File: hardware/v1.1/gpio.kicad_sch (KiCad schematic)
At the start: 23 parts, among them J2 HDMI_C_1.3, U1 ECP5U_12_CABGA256, U5 PCA9306DC1

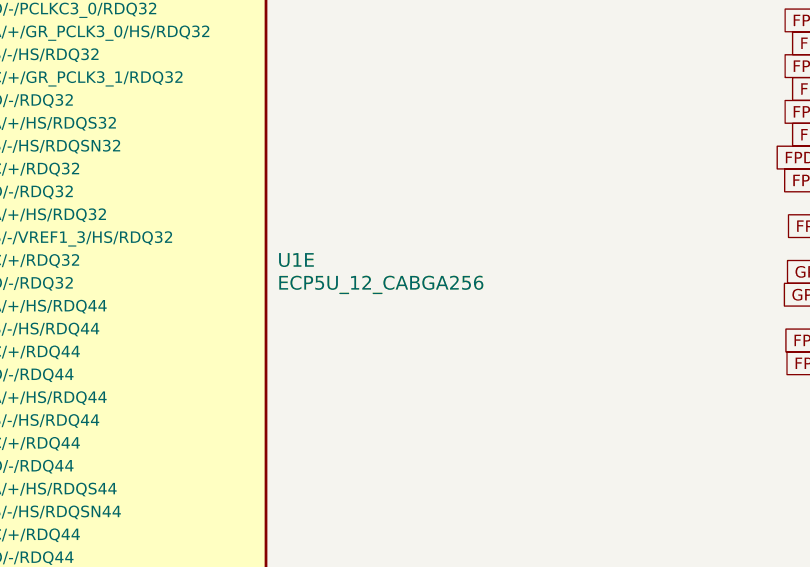
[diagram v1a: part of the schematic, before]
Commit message: Clean up the design by a bit
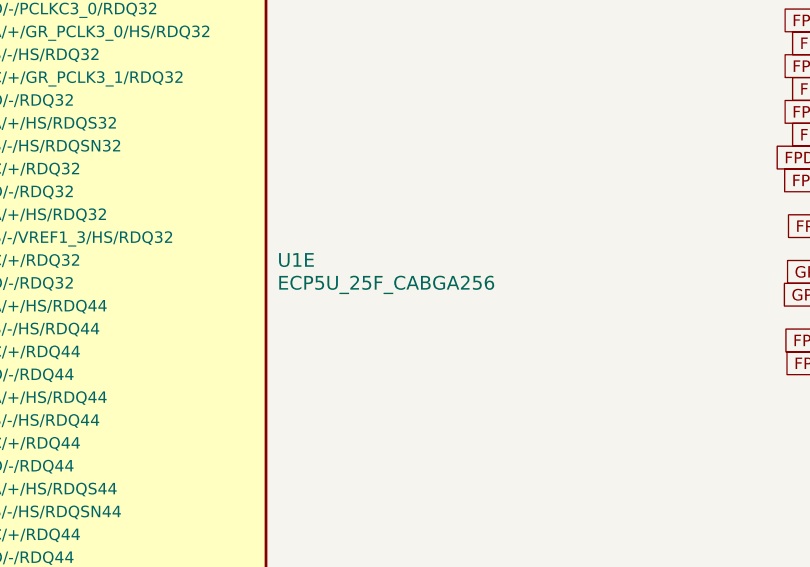
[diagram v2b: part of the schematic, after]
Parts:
- U1: value ECP5U_12_CABGA256 -> ECP5U_25F_CABGA256
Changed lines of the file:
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@@
 			)
 		)
-		(property "Value" "ECP5U_12_CABGA256"
+		(property "Value" "ECP5U_25F_CABGA256"
 			(at 104.14 100.3299 0)
 			(effects

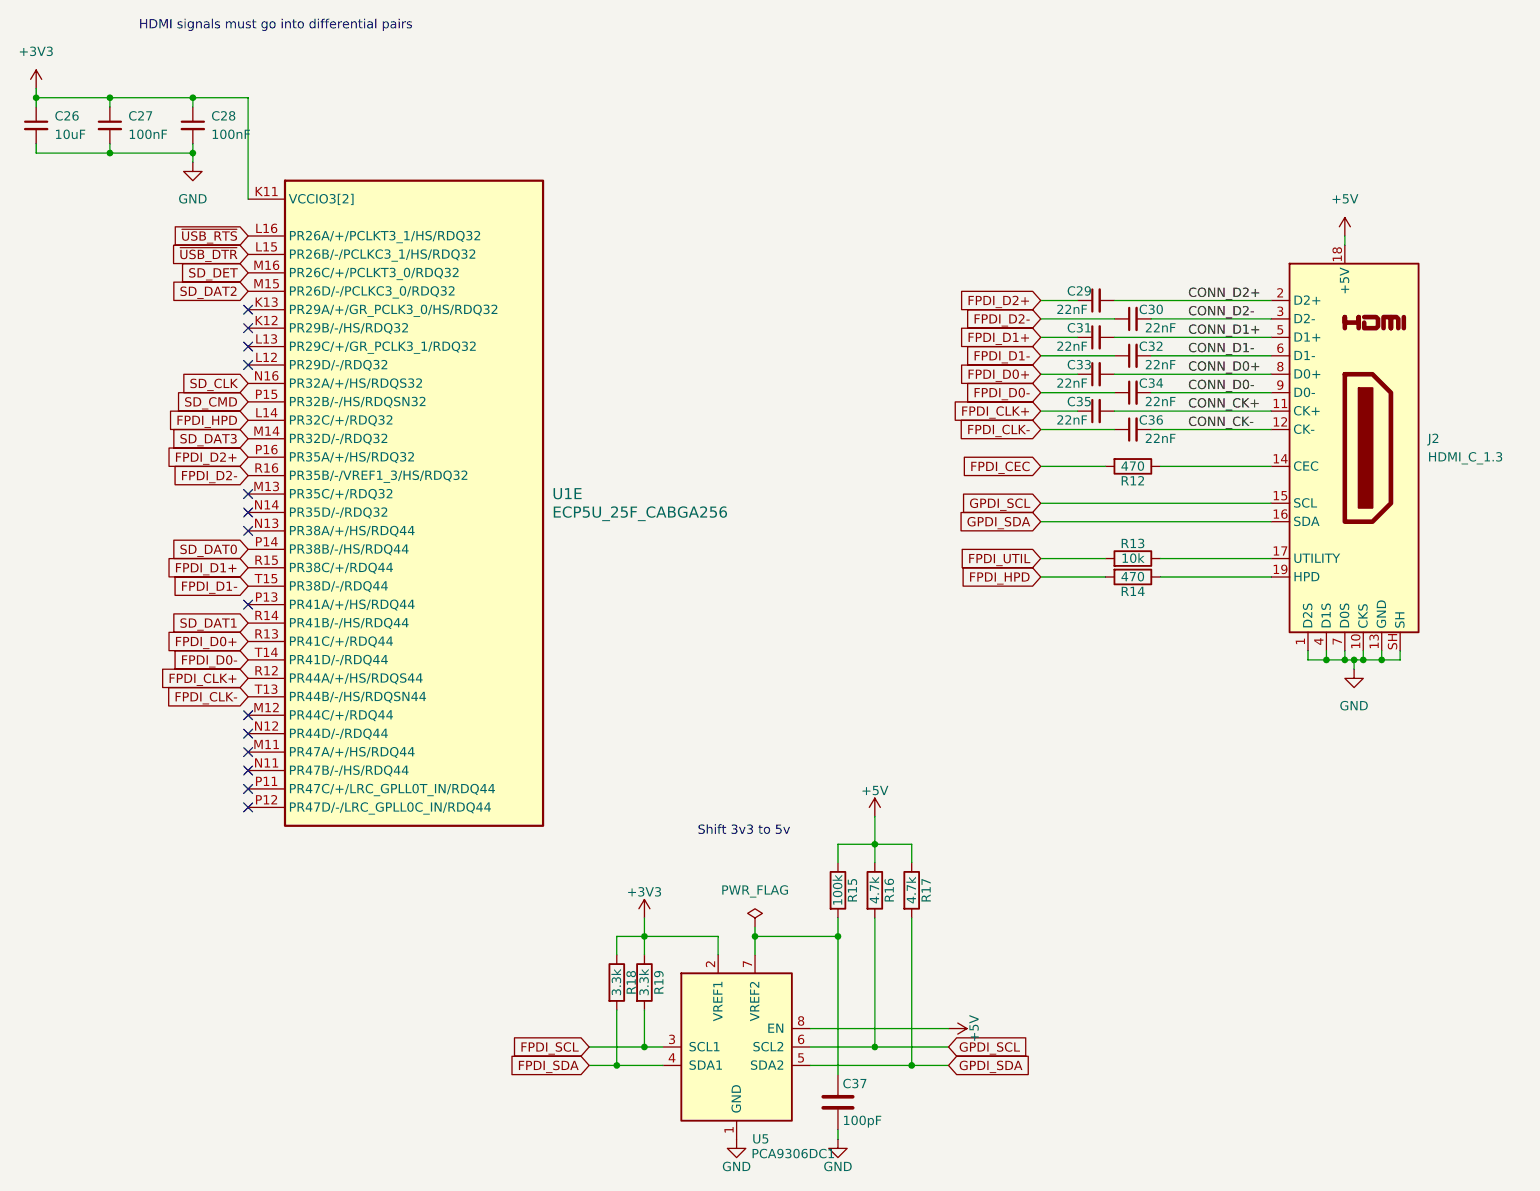
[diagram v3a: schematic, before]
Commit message: Fix pin assignment errors and schematic lable naming mismatch between versions
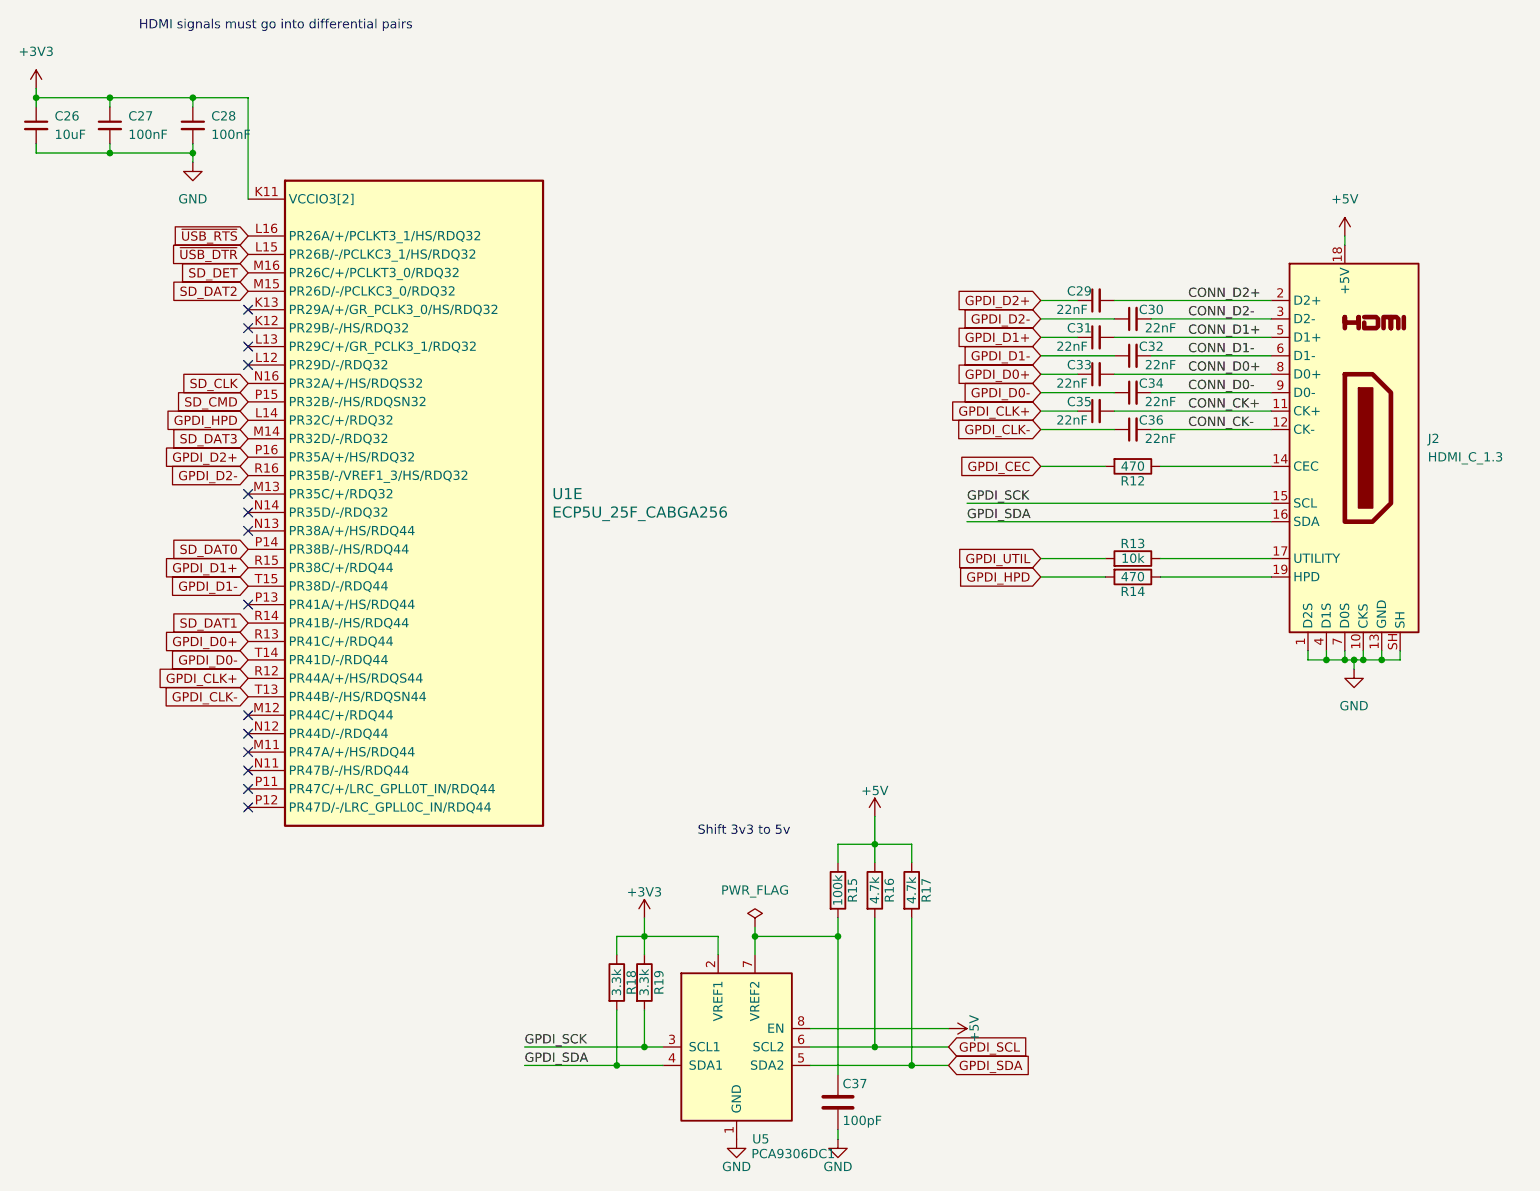
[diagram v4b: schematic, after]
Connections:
- net FPDI_SDA is gone; now on net GPDI_SDA: R18.2, U5.4 (SDA1)
- net GPDI_SCL: no longer J2.15 (SCL)
- net FPDI_CEC renamed GPDI_CEC
- net FPDI_CLK+ renamed GPDI_CLK+
- net FPDI_CLK- renamed GPDI_CLK-
- net FPDI_D0+ renamed GPDI_D0+
- net FPDI_D0- renamed GPDI_D0-
- net FPDI_D1+ renamed GPDI_D1+
- net FPDI_D1- renamed GPDI_D1-
- net FPDI_D2+ renamed GPDI_D2+
- net FPDI_D2- renamed GPDI_D2-
- net FPDI_HPD renamed GPDI_HPD
- net FPDI_SCL renamed GPDI_SCK
- net GPDI_SCK: now also J2.15 (SCL)
- net FPDI_UTIL renamed GPDI_UTIL

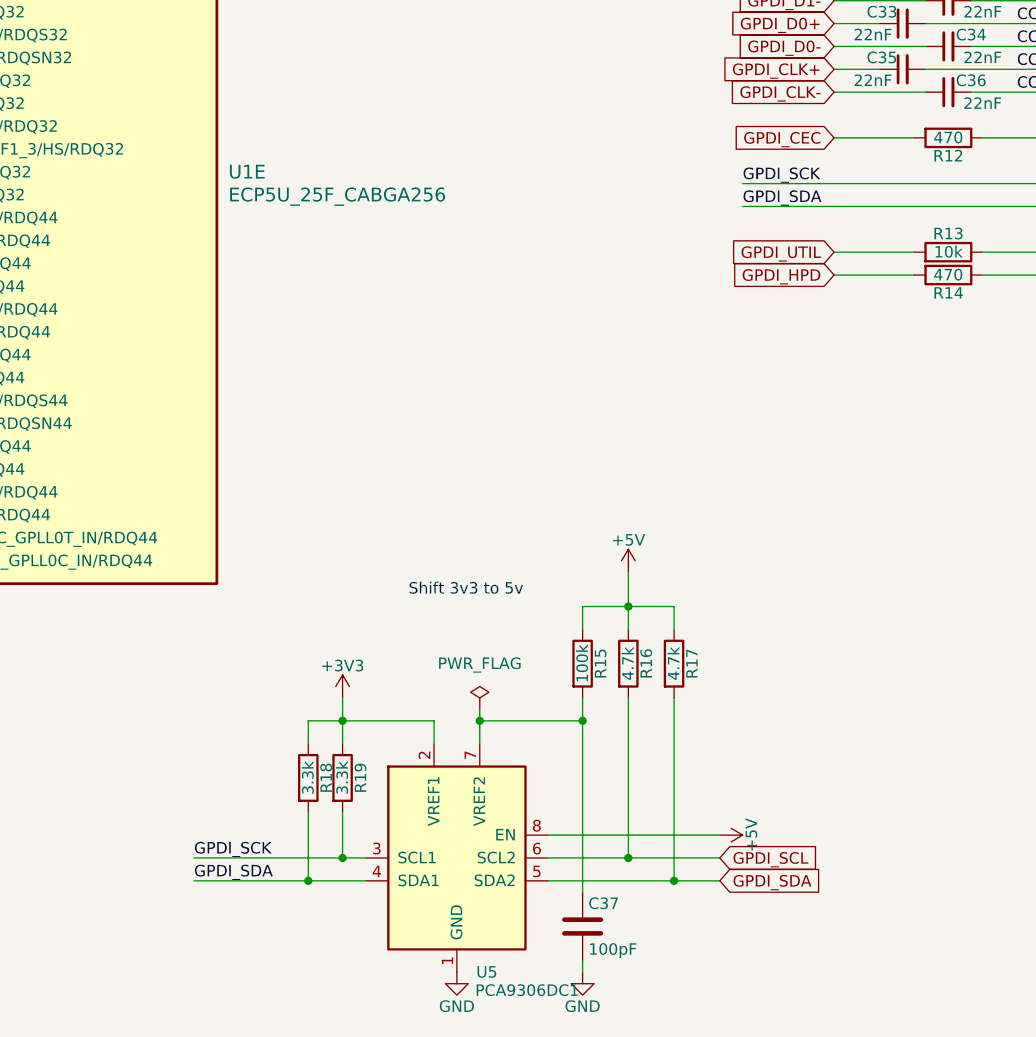
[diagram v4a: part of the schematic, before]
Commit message: Increase pad spacing to 1.9mm and change SCL name to SCK
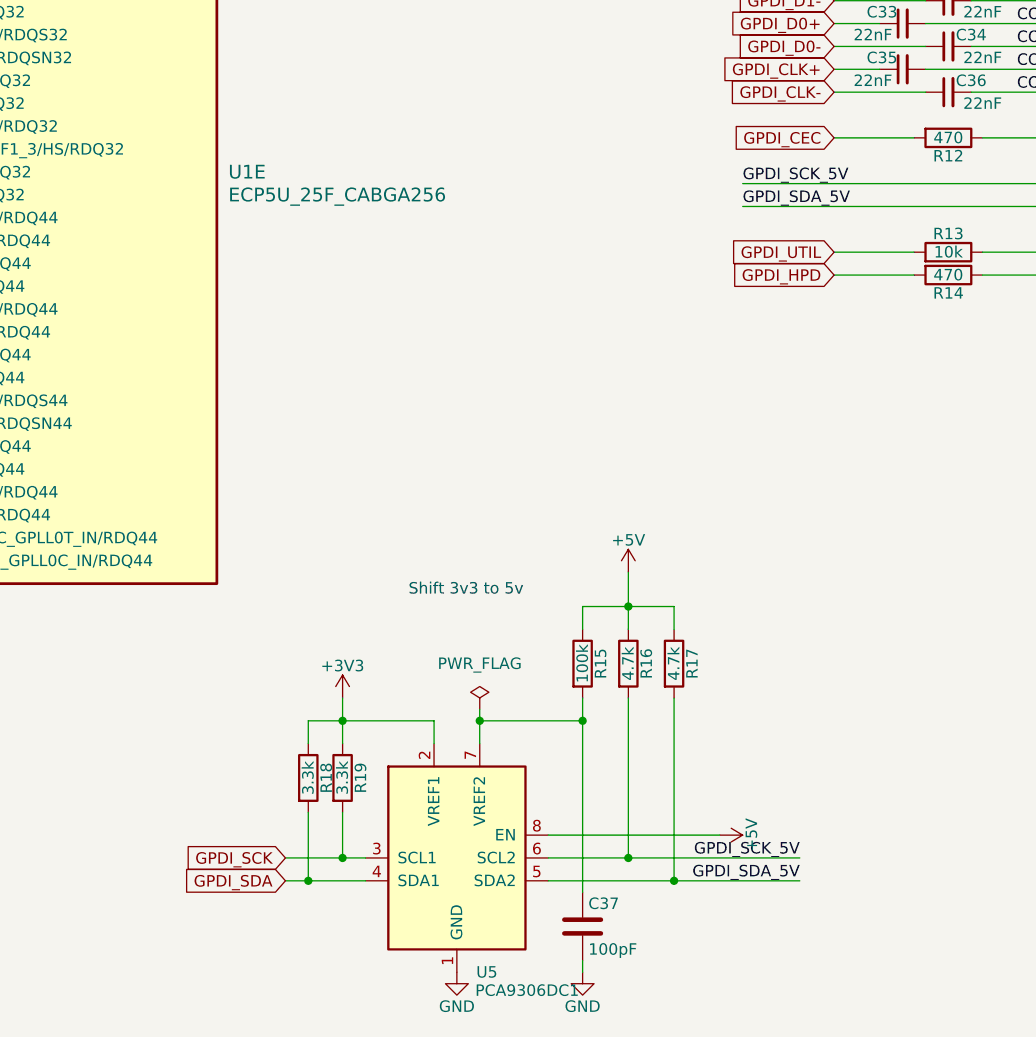
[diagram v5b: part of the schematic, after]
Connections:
- net GPDI_SCK: no longer J2.15 (SCL)
- net GPDI_SDA: no longer J2.16 (SDA), R17.2, U5.5 (SDA2)
- net GPDI_SCL renamed GPDI_SCK_5V
- net GPDI_SCK_5V: now also J2.15 (SCL)
- new net GPDI_SDA_5V: J2.16 (SDA), R17.2, U5.5 (SDA2)
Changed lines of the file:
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@@
 	(title_block
 		(title "Icepi zero")
-		(date "2025-06-06")
+		(date "2025-06-11")
 		(rev "v1.1")
 		(company "Chengyin Yao (cheyao)")
@@
 	)
 	(junction
+		(at 143.51 158.75)
+		(diameter 0)
+		(color 0 0 0 0)
+	)
+	(junction
+		(at 210.82 120.65)
+		(diameter 0)
+		(color 0 0 0 0)
+	)
+	(junction
+		(at 113.03 176.53)
+		(diameter 0)
+		(color 0 0 0 0)
+	)
+	(junction
+		(at 148.59 146.05)
+		(diameter 0)
+		(color 0 0 0 0)
+	)
+	(junction
+		(at 132.08 158.75)
+		(diameter 0)
+		(color 0 0 0 0)
+	)
+	(junction
+		(at 214.63 120.65)
+		(diameter 0)
+		(color 0 0 0 0)
+	)
+	(junction
+		(at 43.18 43.18)
+		(diameter 0)
+		(color 0 0 0 0)
+	)
+	(junction
+		(at 218.44 120.65)
+		(diameter 0)
+		(color 0 0 0 0)
+	)
+	(junction
+		(at 54.61 43.18)
+		(diameter 0)
+		(color 0 0 0 0)
+	)
+	(junction
 		(at 116.84 173.99)
-		(diameter 0)
-		(color 0 0 0 0)
-	)
-	(junction
-		(at 143.51 158.75)
-		(diameter 0)
-		(color 0 0 0 0)
-	)
-	(junction
-		(at 210.82 120.65)
-		(diameter 0)
-		(color 0 0 0 0)
-	)
-	(junction
-		(at 113.03 176.53)
-		(diameter 0)
-		(color 0 0 0 0)
-	)
-	(junction
-		(at 148.59 146.05)
-		(diameter 0)
-		(color 0 0 0 0)
-	)
-	(junction
-		(at 132.08 158.75)
-		(diameter 0)
-		(color 0 0 0 0)
-	)
-	(junction
-		(at 214.63 120.65)
-		(diameter 0)
-		(color 0 0 0 0)
-	)
-	(junction
-		(at 43.18 43.18)
-		(diameter 0)
-		(color 0 0 0 0)
-	)
-	(junction
-		(at 218.44 120.65)
-		(diameter 0)
-		(color 0 0 0 0)
-	)
-	(junction
-		(at 54.61 43.18)
 		(diameter 0)
 		(color 0 0 0 0)
@@
 	(wire
 		(pts
-			(xy 148.59 173.99) (xy 158.75 173.99)
+			(xy 148.59 173.99) (xy 167.64 173.99)
 		)
 		(stroke
@@
 	(wire
 		(pts
-			(xy 153.67 176.53) (xy 158.75 176.53)
-		)
-		(stroke
-			(width 0)
-			(type default)
-		)
-	)
-	(wire
-		(pts
 			(xy 171.45 86.36) (xy 176.53 86.36)
 		)
@@
 	(wire
 		(pts
+			(xy 110.49 176.53) (xy 113.03 176.53)
+		)
+		(stroke
+			(width 0)
+			(type default)
+		)
+	)
+	(wire
+		(pts
 			(xy 218.44 120.65) (xy 220.98 120.65)
 		)
@@
 	(wire
 		(pts
-			(xy 100.33 176.53) (xy 113.03 176.53)
+			(xy 153.67 176.53) (xy 167.64 176.53)
 		)
 		(stroke
@@
 	(wire
 		(pts
+			(xy 110.49 173.99) (xy 116.84 173.99)
+		)
+		(stroke
+			(width 0)
+			(type default)
+		)
+	)
+	(wire
+		(pts
 			(xy 54.61 50.8) (xy 54.61 49.53)
 		)
@@
 	(wire
 		(pts
-			(xy 100.33 173.99) (xy 116.84 173.99)
-		)
-		(stroke
-			(width 0)
-			(type default)
-		)
-	)
-	(wire
-		(pts
 			(xy 153.67 146.05) (xy 153.67 148.59)
 		)
@@
 		)
 	)
-	(label "GPDI_SCK"
-		(at 100.33 173.99 0)
-		(effects
-			(font
-				(size 1.27 1.27)
-			)
-			(justify left bottom)
+	(label "GPDI_SCK_5V"
+		(at 167.64 173.99 180)
+		(effects
+			(font
+				(size 1.27 1.27)
+			)
+			(justify right bottom)
 		)
 	)
@@
 		)
 	)
-	(label "GPDI_SDA"
-		(at 100.33 176.53 0)
-		(effects
-			(font
-				(size 1.27 1.27)
-			)
-			(justify left bottom)
-		)
-	)
-	(label "GPDI_SCK"
+	(label "GPDI_SDA_5V"
+		(at 167.64 176.53 180)
+		(effects
+			(font
+				(size 1.27 1.27)
+			)
+			(justify right bottom)
+		)
+	)
+	(label "GPDI_SCK_5V"
 		(at 161.29 99.06 0)
 		(effects
@@
 		)
 	)
-	(label "GPDI_SDA"
+	(label "GPDI_SDA_5V"
 		(at 161.29 101.6 0)
 		(effects
@@
 	(global_label "GPDI_SDA"
 		(shape input)
-		(at 158.75 176.53 0)
-		(effects
-			(font
-				(size 1.27 1.27)
-			)
-			(justify left)
-		)
-		(property "Intersheetrefs" "${INTERSHEET_REFS}"
-			(at 158.75 176.53 0)
+		(at 110.49 176.53 180)
+		(effects
+			(font
+				(size 1.27 1.27)
+			)
+			(justify right)
+		)
+		(property "Intersheetrefs" "${INTERSHEET_REFS}"
+			(at 110.49 176.53 0)
 			(effects
 				(font
@@
 		)
 	)
-	(global_label "GPDI_SCL"
-		(shape input)
-		(at 158.75 173.99 0)
-		(effects
-			(font
-				(size 1.27 1.27)
-			)
-			(justify left)
-		)
-		(property "Intersheetrefs" "${INTERSHEET_REFS}"
-			(at 158.75 173.99 0)
-			(effects
-				(font
+	(global_label "GPDI_SCK"
+		(shape input)
+		(at 110.49 173.99 180)
+		(effects
+			(font
+				(size 1.27 1.27)
+			)
+			(justify right)
+		)
+		(property "Intersheetrefs" "${INTERSHEET_REFS}"
+			(at 110.49 173.99 0)
+			(effects
+				(font

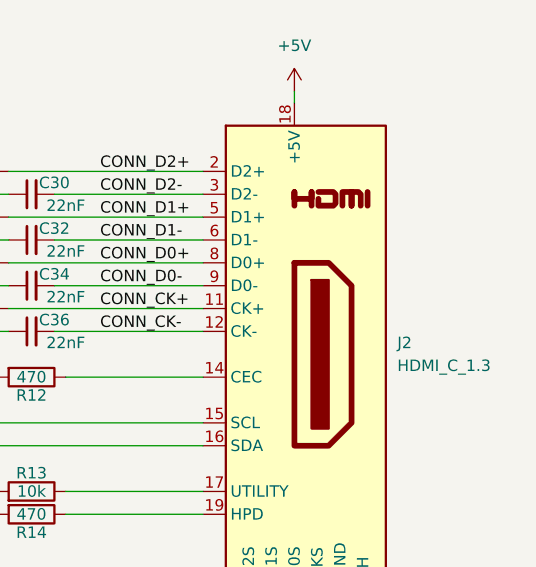
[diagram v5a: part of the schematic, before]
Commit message: Added start of documentation and changed GPDI
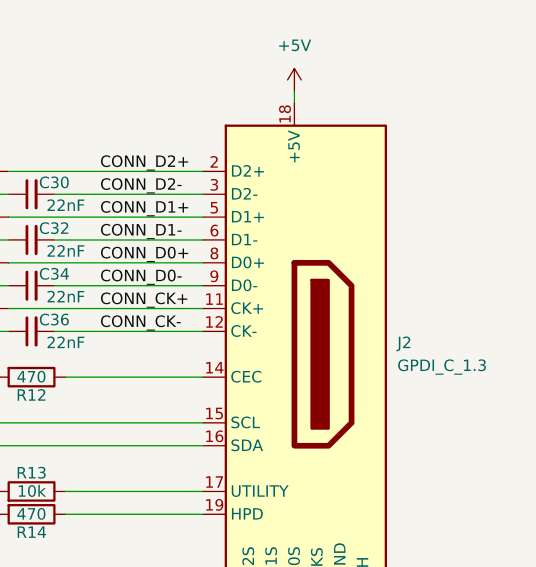
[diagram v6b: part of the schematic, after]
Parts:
- J2: value HDMI_C_1.3 -> GPDI_C_1.3; symbol Connector:HDMI_C_1.3 -> icepi-lib:GPDI_C_1.3; LCSC Link (none) -> https://lcsc.com/product-detail/HDMI-Connectors_XKB-Connect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; Manufactuer Part Number (none) -> A71-05H4-111N1
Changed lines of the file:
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@@
 	)
 	(symbol
-		(lib_id "Connector:HDMI_C_1.3")
+		(lib_id "icepi-lib:GPDI_C_1.3")
 		(at 213.36 91.44 0)
 		(unit 1)
@@
 			)
 		)
-		(property "Value" "HDMI_C_1.3"
+		(property "Value" "GPDI_C_1.3"
 			(at 224.79 92.7099 0)
 			(effects
@@
 			)
 		)
-		(property "Datasheet" "http://pinoutguide.com/PortableDevices/mini_hdmi_pinout.shtml"
+		(property "Datasheet" "-"
 			(at 213.995 91.44 0)
 			(effects
@@
 			)
 		)
-		(property "Description" "HDMI 1.3+ type C connector"
+		(property "Description" "GPDI type C connector"
 			(at 213.36 91.44 0)
 			(effects
@@
 		)
 		(property "LCSC Part #" "C2682170"
+			(at 213.36 91.44 0)
+			(effects
+				(font
+					(size 1.27 1.27)
+				)
+				(hide yes)
+			)
+		)
+		(property "LCSC Link" "https://lcsc.com/product-detail/HDMI-Connectors_XKB-Connection-A71-05H4-111N1_C2682170.html"
+			(at 213.36 91.44 0)
+			(effects
+				(font
+					(size 1.27 1.27)
+				)
+				(hide yes)
+			)
+		)
+		(property "Manufactuer Part Number" "A71-05H4-111N1"
 			(at 213.36 91.44 0)
 			(effects
@@
 		)
 		(instances
-			(project ""
+			(project "icepi-zero"
 				(path "/f88da08e-cf42-4d03-a08f-3f602fe6658d/efe0a411-ae63-4682-aa63-a9a30697cd67"
 					(reference "J2")
